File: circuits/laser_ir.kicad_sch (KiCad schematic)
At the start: 10 parts, among them Q1 AO3400A, U5 TLV9001

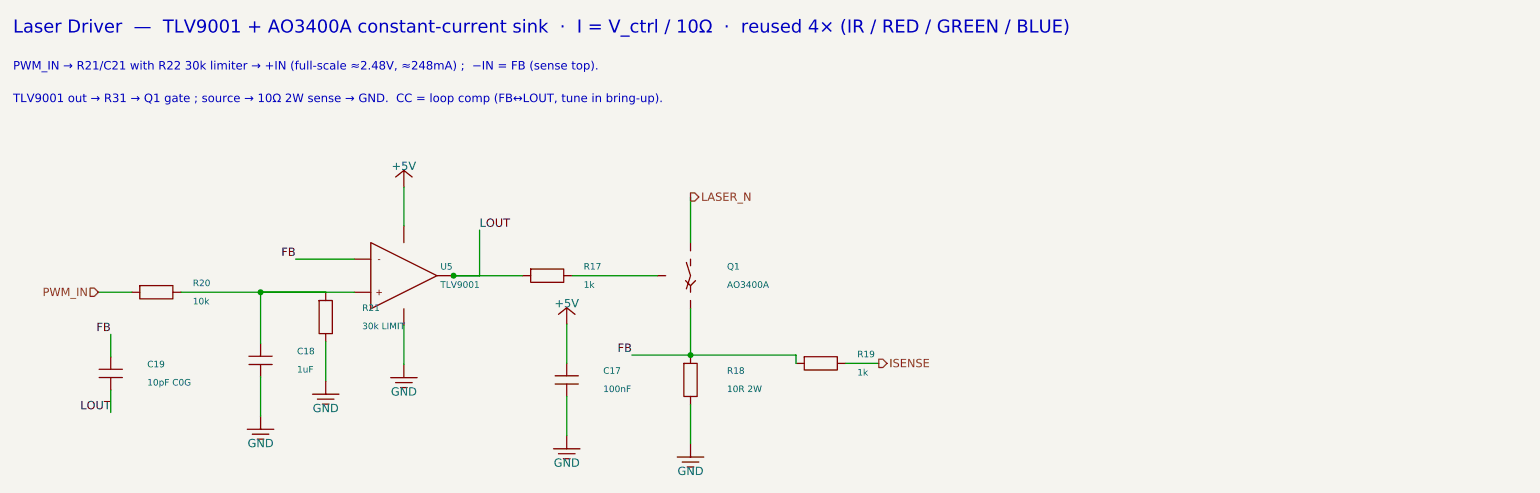
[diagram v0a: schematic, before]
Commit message: chore(circuits): update laser controller release artifacts
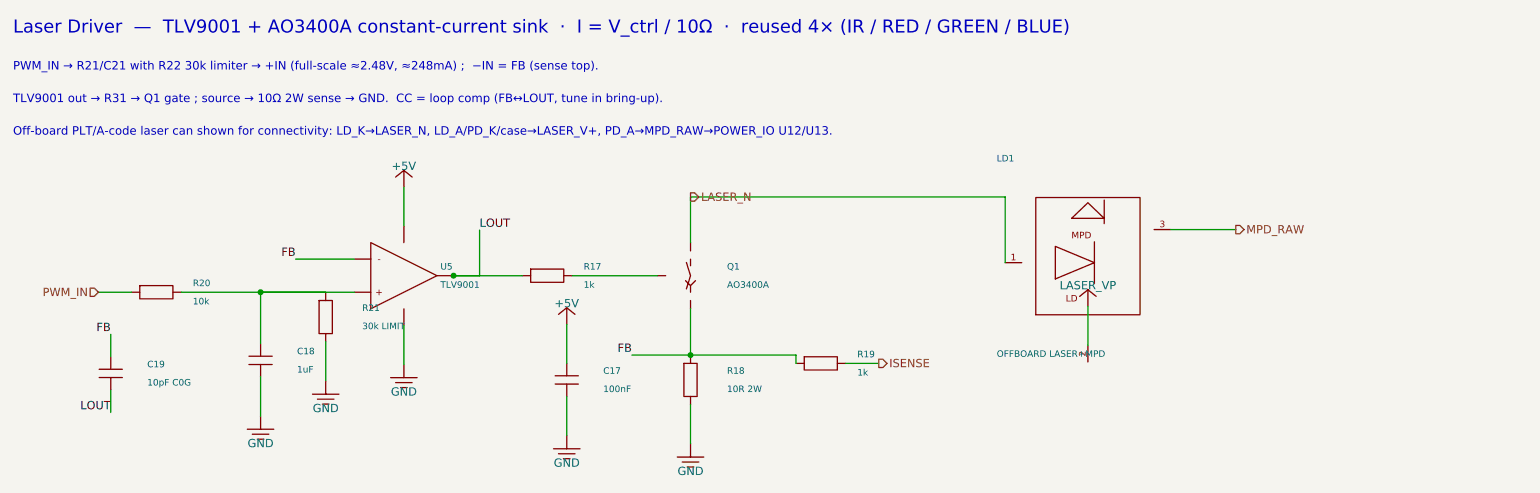
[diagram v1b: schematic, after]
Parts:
- removed Q1: AO3400A, Package_TO_SOT_SMD:SOT-23, symbol viv:NMOS
- added R18: 10R 2W, Resistor_SMD:R_2512_6332Metric_Pad1.40x3.35mm_HandSolder, symbol viv:R_V
- added R20: 10k, Resistor_SMD:R_0603_1608Metric_Pad0.98x0.95mm_HandSolder, symbol viv:R_H
- LD1: renamed from R20; value 10k -> OFFBOARD LASER+MPD; footprint Resistor_SMD:R_0603_1608Metric_Pad0.98x0.95mm_HandSolder -> (none); symbol viv:R_H -> viv:LASER_CAN_MON_PD; LCSC C269701 -> (none); Part Number 0603WAF1002T5E -> (none); now left out of the parts list
- Q1: renamed from R18; value 10R 2W -> AO3400A; footprint Resistor_SMD:R_2512_6332Metric_Pad1.40x3.35mm_HandSolder -> Package_TO_SOT_SMD:SOT-23; symbol viv:R_V -> viv:NMOS; LCSC C5123624 -> C20917; Part Number HoCR2512-2W-10R-1% -> AO3400A
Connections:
- net FB: now also Q1.2 (S), R18.1; no longer Q1.1
- net GND: now also R18.2; no longer Q1.2
- net LASER_N: now also LD1.1 (LD_K), Q1.3 (D)
- net PWM_IN: now also R20.1; no longer LD1.1
- net at C18.1, R21.1, U5.3 (+): now also R20.2; no longer LD1.2
- net at R17.2: now also Q1.1 (G)
- new net LASER_V+: LD1.2 (LD_A/PD_K/CASE)
- new net MPD_RAW: LD1.3 (PD_A)
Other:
- note added: "Off-board PLT/A-code laser can shown for connectivity: LD_K→LASER_N, LD_A/PD_K/case→LASER_V+, PD_A→MPD_RAW→POWER_IO U12/U13."
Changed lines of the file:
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@@
+    )
+  )
+  (symbol (lib_id "viv:LASER_CAN_MON_PD") (at 315 150 0) (unit 1)
+    (in_bom no) (on_board yes) (dnp no)
+    (property "Reference" "LD1" (at 301 134 0) (effects (font (size 1.0 1.0)) (justify left)))
+    (property "Value" "OFFBOARD LASER+MPD" (at 301 164 0) (effects (font (size 1.0 1.0)) (justify left)))
+    (property "Footprint" "" (at 315 150 0) (effects (font (size 1.0 1.0)) hide))
+    (property "Datasheet" "" (at 315 150 0) (effects (font (size 1.0 1.0)) hide))
+    (property "Part Number" "" (at 315 150 0) (effects (font (size 1.0 1.0)) hide))
+    (property "LCSC" "" (at 315 150 0) (effects (font (size 1.0 1.0)) hide))
+    (pin "1")
+    (pin "2")
+    (pin "3")
+    (instances
+      (project "laser_controller"
+        (path "/c1d2e3f4-6000-4000-a000-000000000001" (reference "LD1") (unit 1))
+      )
     )
   )
@@
       (project "laser_controller"
         (path "/c1d2e3f4-6000-4000-a000-000000000001" (reference "#PWR07") (unit 1))
+      )
+    )
+  )
+  (symbol (lib_id "viv:LASER_VP") (at 315 156.7 0) (unit 1)
+    (in_bom no) (on_board yes) (dnp no)
+    (property "Reference" "#PWR08" (at 315 153.7 0) (effects (font (size 1.0 1.0)) hide))
+    (property "Value" "LASER_VP" (at 315 153.5 0) (effects (font (size 1.27 1.27))))
+    (property "Footprint" "" (at 0 0 0) (effects (font (size 1.0 1.0)) hide))
+    (property "Datasheet" "" (at 0 0 0) (effects (font (size 1.0 1.0)) hide))
+    (pin "1")
+    (instances
+      (project "laser_controller"
+        (path "/c1d2e3f4-6000-4000-a000-000000000001" (reference "#PWR08") (unit 1))
       )
     )
@@
   (wire (pts (xy 277.81 165.46) (xy 282.89 165.46)) (stroke (width 0) (type default)))
   (wire (pts (xy 254 146.92) (xy 254 139.92)) (stroke (width 0) (type default)))
+  (wire (pts (xy 254 139.92) (xy 302.3 139.92)) (stroke (width 0) (type default)))
+  (wire (pts (xy 302.3 139.92) (xy 302.3 150)) (stroke (width 0) (type default)))
+  (wire (pts (xy 315 162.7) (xy 315 156.7)) (stroke (width 0) (type default)))
+  (wire (pts (xy 327.7 144.92) (xy 337.7 144.92)) (stroke (width 0) (type default)))
   (wire (pts (xy 202.38 149.46) (xy 193.38 149.46)) (stroke (width 0) (type default)))
   (wire (pts (xy 254 164.19) (xy 245 164.19)) (stroke (width 0) (type default)))
@@
   (hierarchical_label "ISENSE" (shape output) (at 282.89 165.46 0) (effects (font (size 1.27 1.27)) (justify left)))
   (hierarchical_label "LASER_N" (shape output) (at 254 139.92 0) (effects (font (size 1.27 1.27)) (justify left)))
+  (hierarchical_label "MPD_RAW" (shape output) (at 337.7 144.92 0) (effects (font (size 1.27 1.27)) (justify left)))
   (label "FB" (at 193.38 149.46 0) (effects (font (size 1.27 1.27)) (justify right bottom)))
   (label "FB" (at 245 164.19 0) (effects (font (size 1.27 1.27)) (justify right bottom)))
@@
   (text "PWM_IN → R21/C21 with R22 30k limiter → +IN (full-scale ≈2.48V, ≈248mA) ;  −IN = FB (sense top)." (at 150 120 0) (effects (font (size 1.3 1.3)) (justify left)))
   (text "TLV9001 out → R31 → Q1 gate ; source → 10Ω 2W sense → GND.  CC = loop comp (FB↔LOUT, tune in bring-up)." (at 150 125 0) (effects (font (size 1.3 1.3)) (justify left)))
+  (text "Off-board PLT/A-code laser can shown for connectivity: LD_K→LASER_N, LD_A/PD_K/case→LASER_V+, PD_A→MPD_RAW→POWER_IO U12/U13." (at 150 130 0) (effects (font (size 1.3 1.3)) (justify left)))
   (sheet_instances
     (path "/" (page "1"))

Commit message: fix(circuits): import mcu sheet and laser footprints
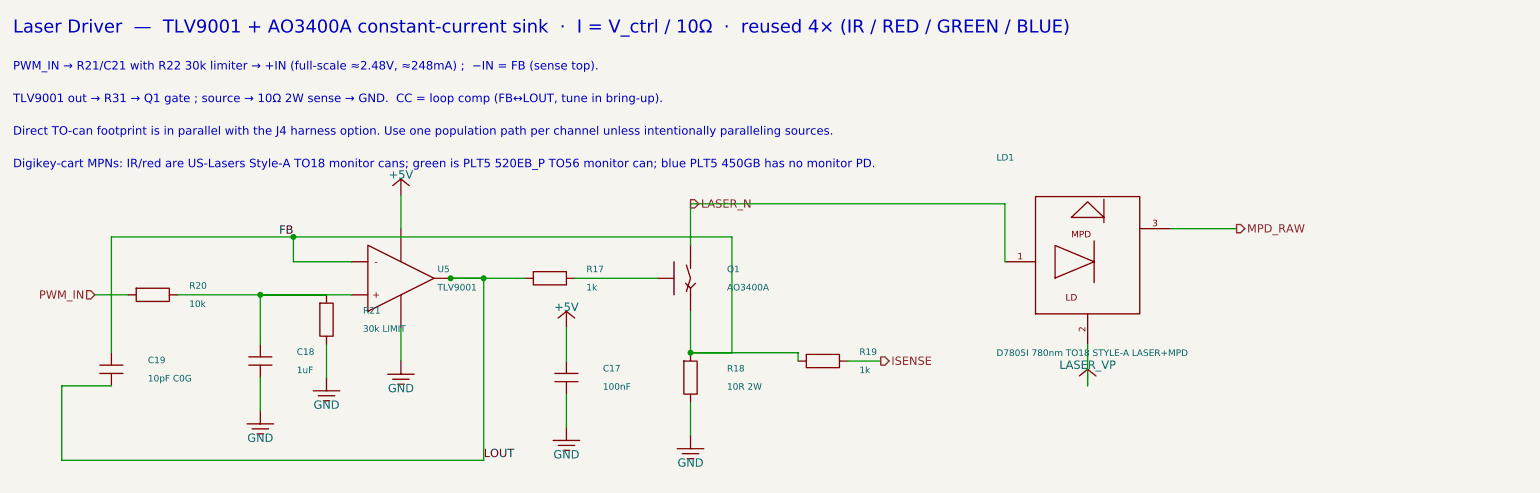
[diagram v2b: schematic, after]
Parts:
- C17: LCSC C1525 -> C83056; Part Number CL05B104KO5NNNC -> 0402B104K160CT
- C18: LCSC C52923 -> C7472946; Part Number CL05A105KA5NQNC -> HGC0402R5105K250NTEJ
- LD1: value OFFBOARD LASER+MPD -> D7805I 780nm TO18 STYLE-A LASER+MPD; footprint (none) -> OptoDevice:LaserDiode_TO18-D5.6-3; Part Number (none) -> D7805I
- R17, R19: LCSC C21190 -> C2907002; Part Number 0603WAF1001T5E -> FRC0603F1001TS
- R20: LCSC C269701 -> C844918; Part Number 0603WAF1002T5E -> CRCW060310K0FKEA
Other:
- note added: "Digikey-cart MPNs: IR/red are US-Lasers Style-A TO18 monitor cans; green is PLT5 520EB_P TO56 monitor can; blue PLT5 450GB has no monitor PD."
- note added: "Direct TO-can footprint is in parallel with the J4 harness option. Use one population path per channel unless intentionally paralleling sources."
- note removed: "Off-board PLT/A-code laser can shown for connectivity: LD_K→LASER_N, LD_A/PD_K/case→LASER_V+, PD_A→MPD_RAW→POWER_IO U12/U13."

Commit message: save laser controller schematic and layout state
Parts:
- removed R20: 10k, Resistor_SMD:R_0603_1608Metric_Pad0.98x0.95mm_HandSolder, symbol viv:R_H
- removed R21: 30k LIMIT, Resistor_SMD:R_0603_1608Metric_Pad0.98x0.95mm_HandSolder, symbol viv:R_V
- added Q1: AO3400A, Package_TO_SOT_SMD:SOT-23, symbol viv:NMOS
- added R17: 1k, Resistor_SMD:R_0603_1608Metric_Pad0.98x0.95mm_HandSolder, symbol viv:R_H
- R20: renamed from R17; value 1k -> 10k; LCSC C2907002 -> C844918; Part Number FRC0603F1001TS -> CRCW060310K0FKEA
- R21: renamed from Q1; value AO3400A -> 30k LIMIT; footprint Package_TO_SOT_SMD:SOT-23 -> Resistor_SMD:R_0603_1608Metric_Pad0.98x0.95mm_HandSolder; symbol viv:NMOS -> viv:R_V; LCSC C20917 -> C22984; Part Number AO3400A -> 0603WAF3002T5E
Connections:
- net FB: now also Q1.2 (S); no longer R21.2 (S)
- net GND: now also R21.2
- net LASER_N: now also Q1.3 (D); no longer R21.3 (D)
- net LOUT: now also R17.1; no longer R20.1
- net PWM_IN: now also R20.1
- net at C18.1, U5.3 (+): now also R20.2, R21.1
- new net: Q1.1 (G), R17.2
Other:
- moved on the sheet: R20

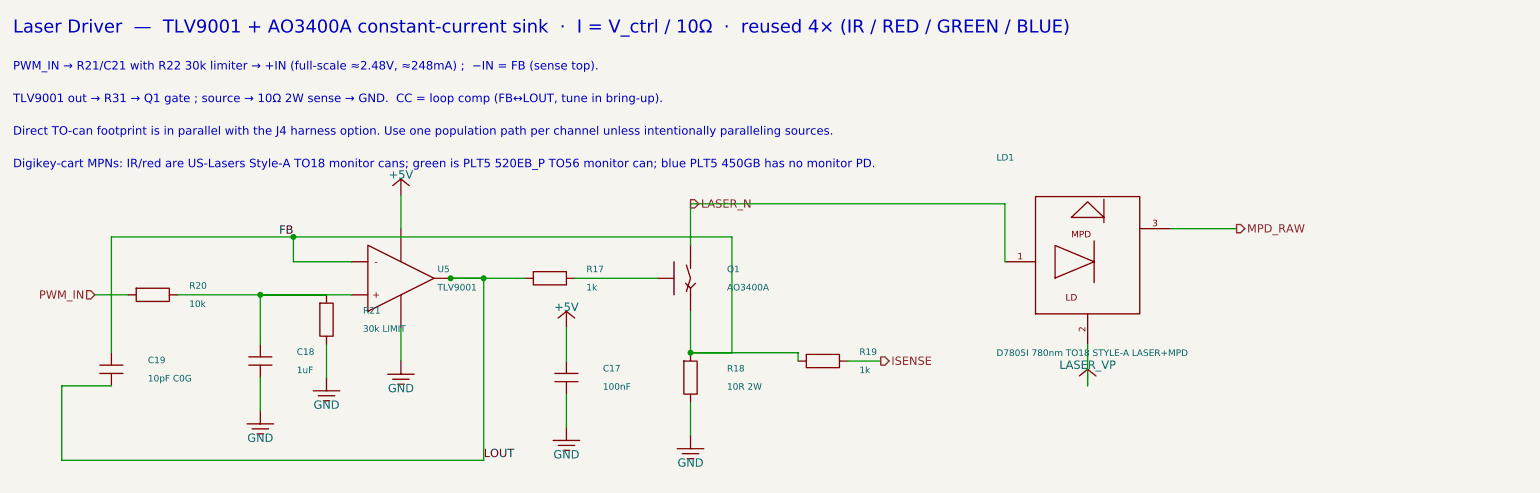
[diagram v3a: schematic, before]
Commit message: save current laser controller recovery state
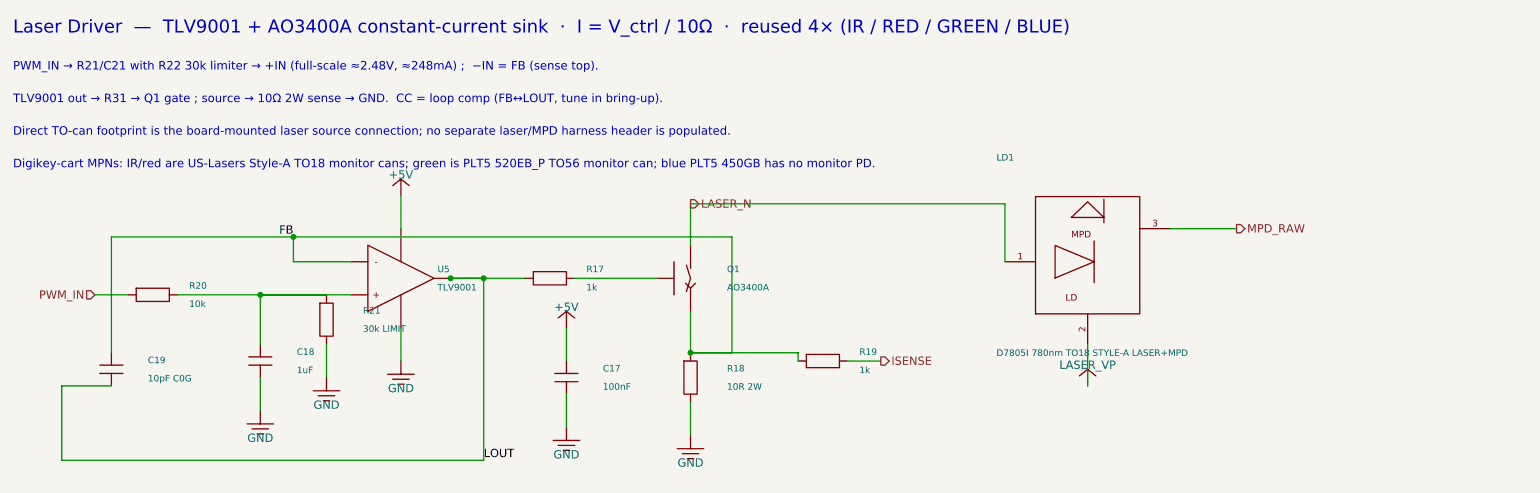
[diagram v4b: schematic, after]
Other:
- note added: "Direct TO-can footprint is the board-mounted laser source connection; no separate laser/MPD harness header is populated."
- note removed: "Direct TO-can footprint is in parallel with the J4 harness option. Use one population path per channel unless intentionally paralleling sources."
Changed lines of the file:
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@@
   (text "PWM_IN → R21/C21 with R22 30k limiter → +IN (full-scale ≈2.48V, ≈248mA) ;  −IN = FB (sense top)." (at 150 120 0) (effects (font (size 1.3 1.3)) (justify left)))
   (text "TLV9001 out → R31 → Q1 gate ; source → 10Ω 2W sense → GND.  CC = loop comp (FB↔LOUT, tune in bring-up)." (at 150 125 0) (effects (font (size 1.3 1.3)) (justify left)))
-  (text "Direct TO-can footprint is in parallel with the J4 harness option. Use one population path per channel unless intentionally paralleling sources." (at 150 130 0) (effects (font (size 1.3 1.3)) (justify left)))
+  (text "Direct TO-can footprint is the board-mounted laser source connection; no separate laser/MPD harness header is populated." (at 150 130 0) (effects (font (size 1.3 1.3)) (justify left)))
   (text "Digikey-cart MPNs: IR/red are US-Lasers Style-A TO18 monitor cans; green is PLT5 520EB_P TO56 monitor can; blue PLT5 450GB has no monitor PD." (at 150 135 0) (effects (font (size 1.3 1.3)) (justify left)))
   (sheet_instances
